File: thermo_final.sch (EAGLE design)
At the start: 113 parts

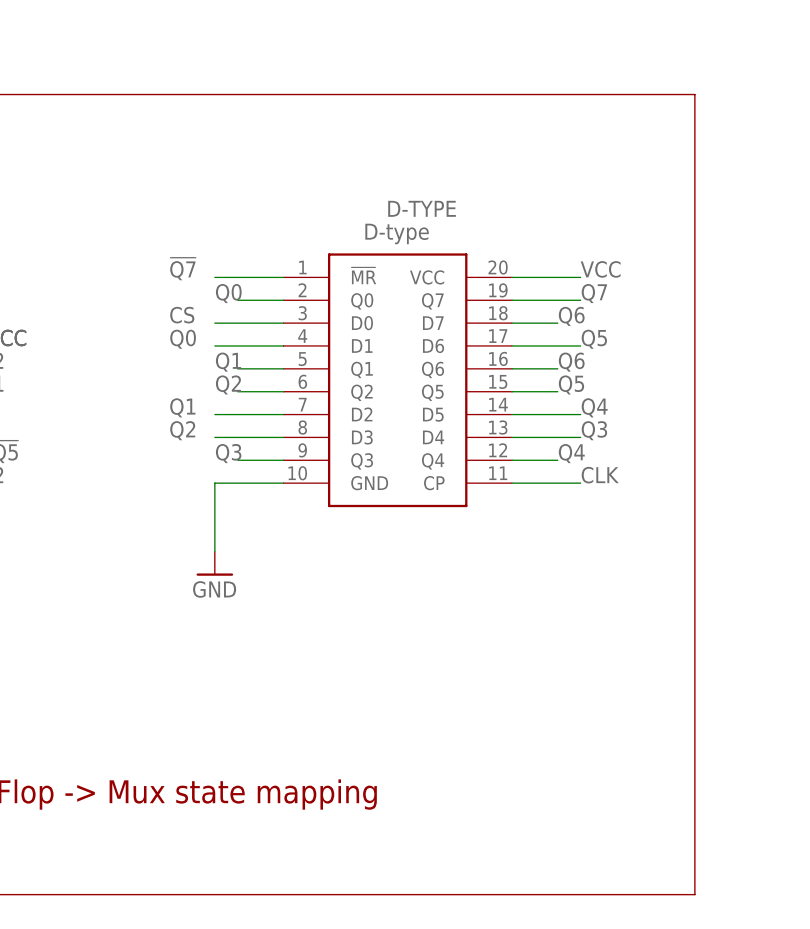
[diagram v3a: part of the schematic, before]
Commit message: Fixed Flip-Flop Footprint/Pushed 3D Model
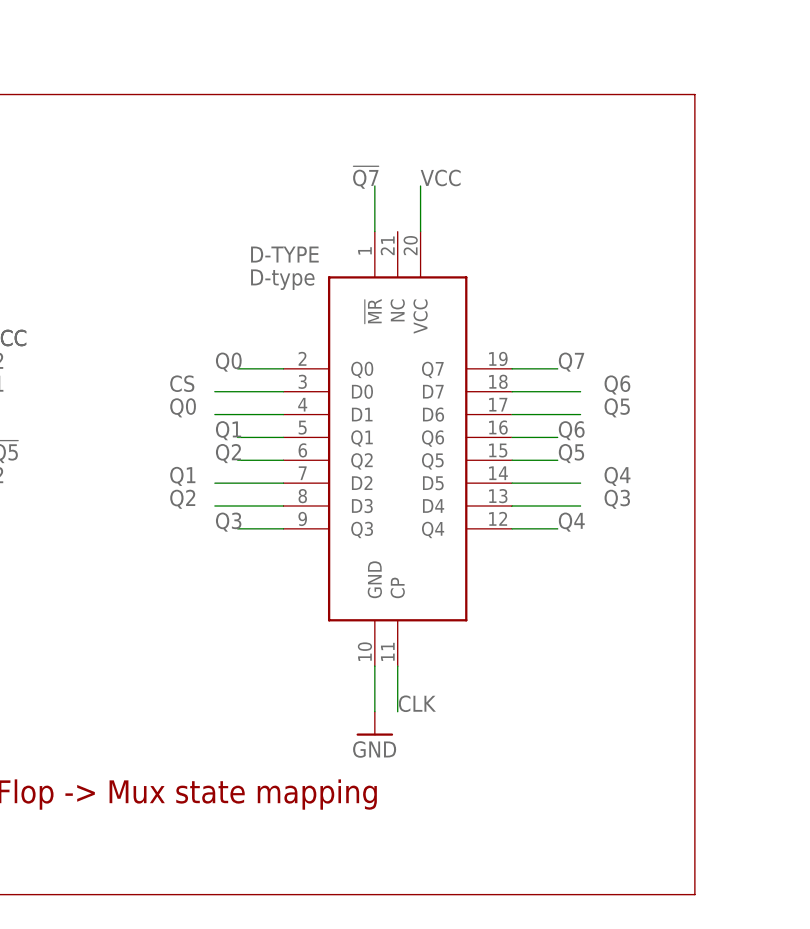
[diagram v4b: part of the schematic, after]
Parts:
- D-TYPE: device SamacSys_Parts:74AHCT273D,118 -> SamacSys_Parts:74AHC273BQ,115
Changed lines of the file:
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@@
 <part name="C1" library="SamacSys_Parts" library_urn="urn:adsk.eagle:library:34728992" deviceset="CGA3E2X7R1H104K080AE" device="" package3d_urn="urn:adsk.eagle:package:34729062/3" value="0.1uF"/>
 <part name="GND3" library="supply1" library_urn="urn:adsk.eagle:library:371" deviceset="GND" device=""/>
-<part name="D-TYPE" library="SamacSys_Parts" library_urn="urn:adsk.eagle:library:34728992" deviceset="74AHCT273D,118" device="" package3d_urn="urn:adsk.eagle:package:34729072/2" value="D-type"/>
+<part name="D-TYPE" library="SamacSys_Parts" library_urn="urn:adsk.eagle:library:34728992" deviceset="74AHC273BQ,115" device="" package3d_urn="urn:adsk.eagle:package:35179643/2" value="D-type"/>
 <part name="AND2" library="SamacSys_Parts" library_urn="urn:adsk.eagle:library:34728992" deviceset="SN74LVC08AMDREP" device="" package3d_urn="urn:adsk.eagle:package:34729073/2" value="AND1"/>
 <part name="GND5" library="supply1" library_urn="urn:adsk.eagle:library:371" deviceset="GND" device=""/>
@@
 <attribute name="VALUE" x="177.8" y="-22.86" size="1.778" layer="96"/>
 </instance>
-<instance part="D-TYPE" gate="G$1" x="15.24" y="-109.22" smashed="yes">
-<attribute name="NAME" x="26.67" y="-101.6" size="1.778" layer="95" align="center-left"/>
-<attribute name="VALUE" x="24.13" y="-104.14" size="1.778" layer="96" align="center-left"/>
+<instance part="D-TYPE" gate="G$1" x="15.24" y="-119.38" smashed="yes">
+<attribute name="NAME" x="11.43" y="-106.68" size="1.778" layer="95" align="center-left"/>
+<attribute name="VALUE" x="11.43" y="-109.22" size="1.778" layer="96" align="center-left"/>
 </instance>
 <instance part="AND2" gate="G$1" x="-114.3" y="-99.06" smashed="yes">
@@
 <attribute name="VALUE" x="-124.46" y="-127" size="1.778" layer="96"/>
 </instance>
-<instance part="GND6" gate="1" x="7.62" y="-142.24" smashed="yes">
-<attribute name="VALUE" x="5.08" y="-144.78" size="1.778" layer="96"/>
+<instance part="GND6" gate="1" x="25.4" y="-160.02" smashed="yes">
+<attribute name="VALUE" x="22.86" y="-162.56" size="1.778" layer="96"/>
 </instance>
 <instance part="INVERTER" gate="G$1" x="-172.72" y="-116.84" smashed="yes">
@@
 <segment>
 <pinref part="D-TYPE" gate="G$1" pin="GND"/>
-<wire x1="15.24" y1="-132.08" x2="7.62" y2="-132.08" width="0.1524" layer="91"/>
-<wire x1="7.62" y1="-132.08" x2="7.62" y2="-139.7" width="0.1524" layer="91"/>
+<wire x1="25.4" y1="-152.4" x2="25.4" y2="-157.48" width="0.1524" layer="91"/>
 <pinref part="GND6" gate="1" pin="GND"/>
 </segment>
@@
 <segment>
 <pinref part="D-TYPE" gate="G$1" pin="VCC"/>
-<wire x1="40.64" y1="-109.22" x2="48.26" y2="-109.22" width="0.1524" layer="91"/>
-<label x="48.26" y="-109.22" size="1.778" layer="95"/>
+<wire x1="30.48" y1="-104.14" x2="30.48" y2="-99.06" width="0.1524" layer="91"/>
+<label x="30.48" y="-99.06" size="1.778" layer="95"/>
 </segment>
 <segment>
@@
 <segment>
 <pinref part="D-TYPE" gate="G$1" pin="CP"/>
-<wire x1="40.64" y1="-132.08" x2="48.26" y2="-132.08" width="0.1524" layer="91"/>
-<label x="48.26" y="-132.08" size="1.778" layer="95"/>
+<wire x1="27.94" y1="-152.4" x2="27.94" y2="-157.48" width="0.1524" layer="91"/>
+<label x="27.94" y="-157.48" size="1.778" layer="95"/>
 </segment>
 <segment>
@@
 <segment>
 <pinref part="D-TYPE" gate="G$1" pin="D0"/>
-<wire x1="15.24" y1="-114.3" x2="7.62" y2="-114.3" width="0.1524" layer="91"/>
-<label x="2.54" y="-114.3" size="1.778" layer="95"/>
+<wire x1="15.24" y1="-121.92" x2="7.62" y2="-121.92" width="0.1524" layer="91"/>
+<label x="2.54" y="-121.92" size="1.778" layer="95"/>
 </segment>
 <segment>
@@
 <segment>
 <pinref part="D-TYPE" gate="G$1" pin="D7"/>
-<wire x1="40.64" y1="-114.3" x2="45.72" y2="-114.3" width="0.1524" layer="91"/>
-<label x="45.72" y="-114.3" size="1.778" layer="95"/>
+<wire x1="40.64" y1="-121.92" x2="48.26" y2="-121.92" width="0.1524" layer="91"/>
+<label x="50.8" y="-121.92" size="1.778" layer="95"/>
 </segment>
 <segment>
 <pinref part="D-TYPE" gate="G$1" pin="Q6"/>
-<wire x1="40.64" y1="-119.38" x2="45.72" y2="-119.38" width="0.1524" layer="91"/>
-<label x="45.72" y="-119.38" size="1.778" layer="95"/>
+<wire x1="40.64" y1="-127" x2="45.72" y2="-127" width="0.1524" layer="91"/>
+<label x="45.72" y="-127" size="1.778" layer="95"/>
 </segment>
 <segment>
@@
 <segment>
 <pinref part="D-TYPE" gate="G$1" pin="D6"/>
-<wire x1="40.64" y1="-116.84" x2="48.26" y2="-116.84" width="0.1524" layer="91"/>
-<label x="48.26" y="-116.84" size="1.778" layer="95"/>
+<wire x1="40.64" y1="-124.46" x2="48.26" y2="-124.46" width="0.1524" layer="91"/>
+<label x="50.8" y="-124.46" size="1.778" layer="95"/>
 </segment>
 <segment>
 <pinref part="D-TYPE" gate="G$1" pin="Q5"/>
-<wire x1="40.64" y1="-121.92" x2="45.72" y2="-121.92" width="0.1524" layer="91"/>
-<label x="45.72" y="-121.92" size="1.778" layer="95"/>
+<wire x1="40.64" y1="-129.54" x2="45.72" y2="-129.54" width="0.1524" layer="91"/>
+<label x="45.72" y="-129.54" size="1.778" layer="95"/>
 </segment>
 <segment>
@@
 <segment>
 <pinref part="D-TYPE" gate="G$1" pin="D5"/>
-<wire x1="40.64" y1="-124.46" x2="48.26" y2="-124.46" width="0.1524" layer="91"/>
-<label x="48.26" y="-124.46" size="1.778" layer="95"/>
+<wire x1="40.64" y1="-132.08" x2="48.26" y2="-132.08" width="0.1524" layer="91"/>
+<label x="50.8" y="-132.08" size="1.778" layer="95"/>
 </segment>
 <segment>
 <pinref part="D-TYPE" gate="G$1" pin="Q4"/>
-<wire x1="40.64" y1="-129.54" x2="45.72" y2="-129.54" width="0.1524" layer="91"/>
-<label x="45.72" y="-129.54" size="1.778" layer="95"/>
+<wire x1="40.64" y1="-137.16" x2="45.72" y2="-137.16" width="0.1524" layer="91"/>
+<label x="45.72" y="-137.16" size="1.778" layer="95"/>
 </segment>
 <segment>
@@
 <segment>
 <pinref part="D-TYPE" gate="G$1" pin="D4"/>
-<wire x1="40.64" y1="-127" x2="48.26" y2="-127" width="0.1524" layer="91"/>
-<label x="48.26" y="-127" size="1.778" layer="95"/>
+<wire x1="40.64" y1="-134.62" x2="48.26" y2="-134.62" width="0.1524" layer="91"/>
+<label x="50.8" y="-134.62" size="1.778" layer="95"/>
 </segment>
 <segment>
 <pinref part="D-TYPE" gate="G$1" pin="Q3"/>
-<wire x1="15.24" y1="-129.54" x2="10.16" y2="-129.54" width="0.1524" layer="91"/>
-<label x="7.62" y="-129.54" size="1.778" layer="95"/>
+<wire x1="15.24" y1="-137.16" x2="10.16" y2="-137.16" width="0.1524" layer="91"/>
+<label x="7.62" y="-137.16" size="1.778" layer="95"/>
 </segment>
 <segment>
@@
 <segment>
 <pinref part="D-TYPE" gate="G$1" pin="D1"/>
-<wire x1="15.24" y1="-116.84" x2="7.62" y2="-116.84" width="0.1524" layer="91"/>
-<label x="2.54" y="-116.84" size="1.778" layer="95"/>
+<wire x1="15.24" y1="-124.46" x2="7.62" y2="-124.46" width="0.1524" layer="91"/>
+<label x="2.54" y="-124.46" size="1.778" layer="95"/>
 </segment>
 <segment>
 <pinref part="D-TYPE" gate="G$1" pin="Q0"/>
-<wire x1="15.24" y1="-111.76" x2="10.16" y2="-111.76" width="0.1524" layer="91"/>
-<label x="7.62" y="-111.76" size="1.778" layer="95"/>
+<wire x1="15.24" y1="-119.38" x2="10.16" y2="-119.38" width="0.1524" layer="91"/>
+<label x="7.62" y="-119.38" size="1.778" layer="95"/>
 </segment>
 <segment>
@@
 <segment>
 <pinref part="D-TYPE" gate="G$1" pin="D2"/>
-<wire x1="15.24" y1="-124.46" x2="7.62" y2="-124.46" width="0.1524" layer="91"/>
-<label x="2.54" y="-124.46" size="1.778" layer="95"/>
+<wire x1="15.24" y1="-132.08" x2="7.62" y2="-132.08" width="0.1524" layer="91"/>
+<label x="2.54" y="-132.08" size="1.778" layer="95"/>
 </segment>
 <segment>
 <pinref part="D-TYPE" gate="G$1" pin="Q1"/>
-<wire x1="15.24" y1="-119.38" x2="10.16" y2="-119.38" width="0.1524" layer="91"/>
-<label x="7.62" y="-119.38" size="1.778" layer="95"/>
+<wire x1="15.24" y1="-127" x2="10.16" y2="-127" width="0.1524" layer="91"/>
+<label x="7.62" y="-127" size="1.778" layer="95"/>
 </segment>
 <segment>
@@
 <segment>
 <pinref part="D-TYPE" gate="G$1" pin="D3"/>
-<wire x1="15.24" y1="-127" x2="7.62" y2="-127" width="0.1524" layer="91"/>
-<label x="2.54" y="-127" size="1.778" layer="95"/>
+<wire x1="15.24" y1="-134.62" x2="7.62" y2="-134.62" width="0.1524" layer="91"/>
+<label x="2.54" y="-134.62" size="1.778" layer="95"/>
 </segment>
 <segment>
 <pinref part="D-TYPE" gate="G$1" pin="Q2"/>
-<wire x1="15.24" y1="-121.92" x2="10.16" y2="-121.92" width="0.1524" layer="91"/>
-<label x="7.62" y="-121.92" size="1.778" layer="95"/>
+<wire x1="15.24" y1="-129.54" x2="10.16" y2="-129.54" width="0.1524" layer="91"/>
+<label x="7.62" y="-129.54" size="1.778" layer="95"/>
 </segment>
 <segment>
@@
 <segment>
 <pinref part="D-TYPE" gate="G$1" pin="Q7"/>
-<wire x1="40.64" y1="-111.76" x2="48.26" y2="-111.76" width="0.1524" layer="91"/>
-<label x="48.26" y="-111.76" size="1.778" layer="95"/>
+<wire x1="40.64" y1="-119.38" x2="45.72" y2="-119.38" width="0.1524" layer="91"/>
+<label x="45.72" y="-119.38" size="1.778" layer="95"/>
 </segment>
 <segment>
@@
 <segment>
 <pinref part="D-TYPE" gate="G$1" pin="!MR"/>
-<wire x1="15.24" y1="-109.22" x2="7.62" y2="-109.22" width="0.1524" layer="91"/>
-<label x="2.54" y="-109.22" size="1.778" layer="95"/>
-</segment>
-</net>
+<wire x1="25.4" y1="-104.14" x2="25.4" y2="-99.06" width="0.1524" layer="91"/>
+<label x="22.86" y="-99.06" size="1.778" layer="95"/>
+</segment>
+</net>

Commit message: Added CMRR Caps at CJ input (Finalized)
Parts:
- added C11, C12: 06035C270JAT2A, SamacSys_Parts:06035C270JAT2A
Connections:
- net CJ+: now also C12.1
- net CJ-: now also C11.2
- net GND: now also C11.1, C12.2
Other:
- note added: "CMRR Aliasing Filter"
- moved on the sheet: AND1, AND2, C1, C10, C2, C3, C4, C5, C6, C7, C8, C9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

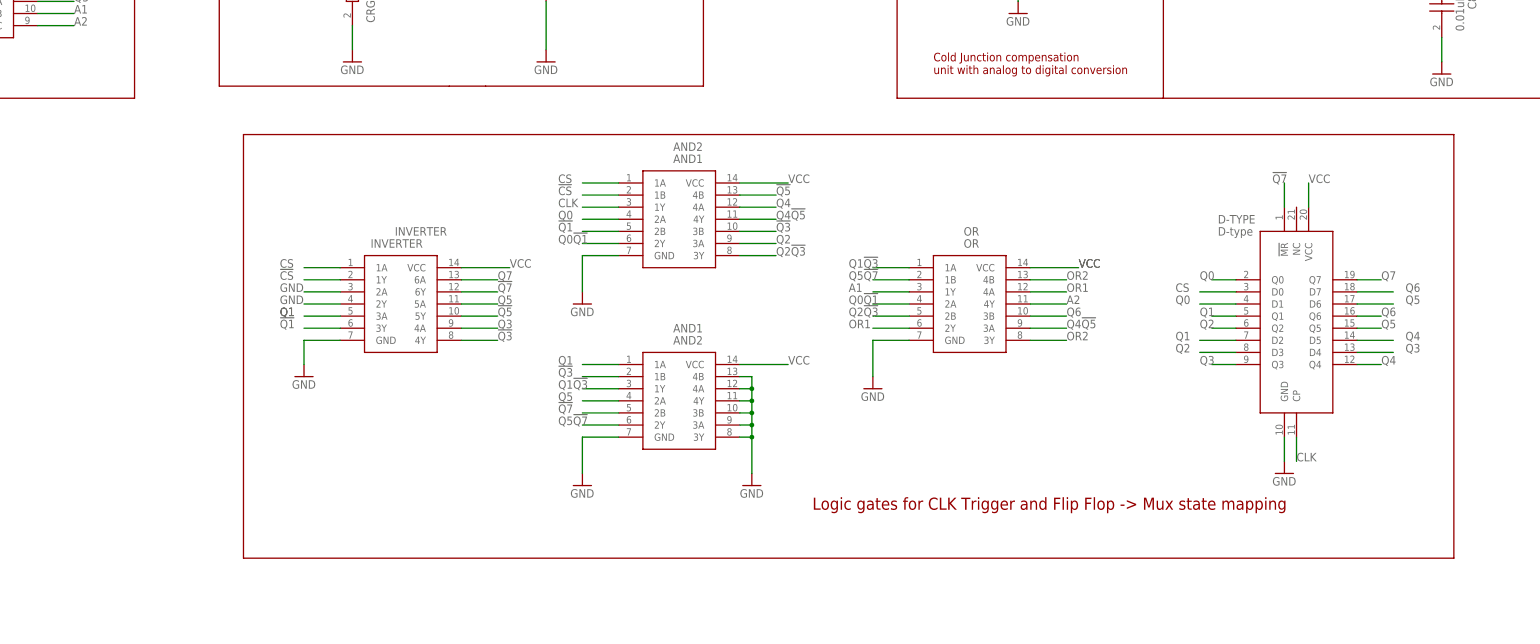
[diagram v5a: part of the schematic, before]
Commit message: Final board/3d model with delay trigger fix
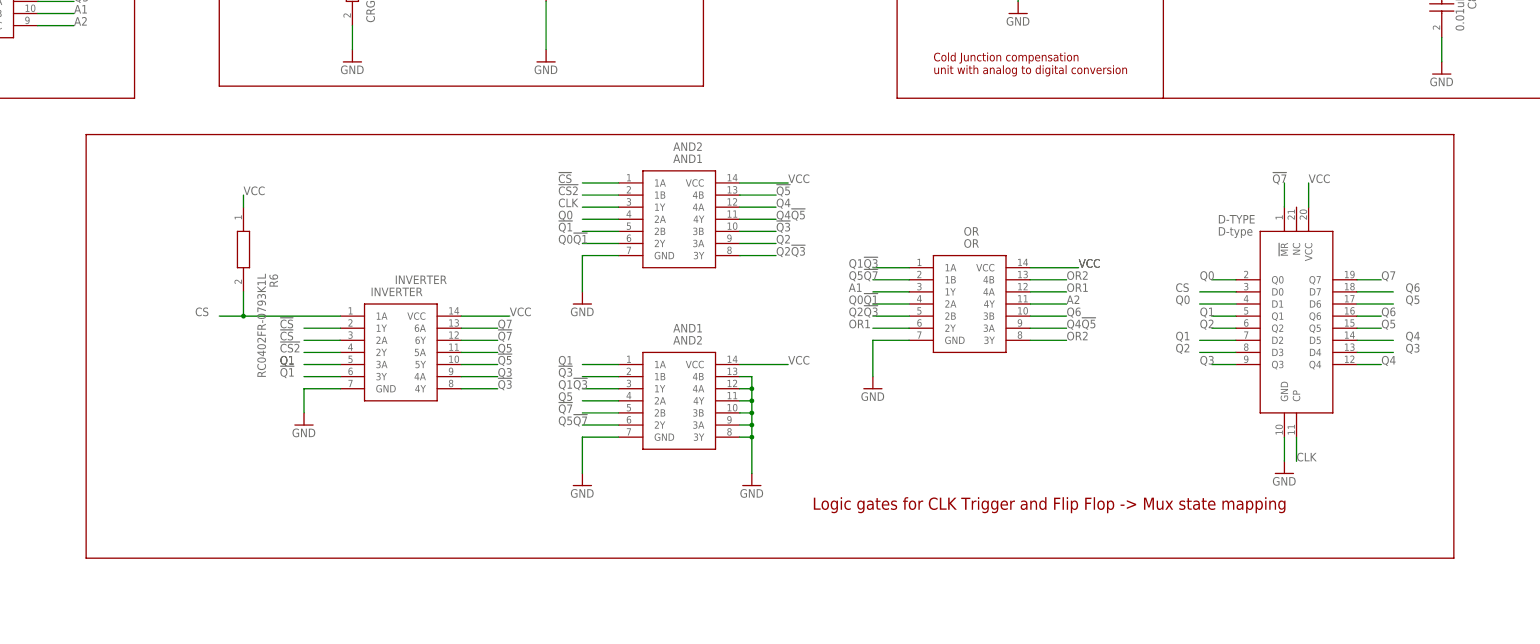
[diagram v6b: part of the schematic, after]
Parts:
- added R6: RC0402FR-0793K1L, SamacSys_Parts:RC0402FR-0793K1L
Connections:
- new net !CS2: AND2.1B, INVERTER.2Y
- net !CS: now also AND2.1A, INVERTER.2A; no longer AND2.1B
- net CS: now also R6.2; no longer AND2.1A
- net GND: no longer INVERTER.2A, INVERTER.2Y
- net VCC: now also R6.1
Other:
- moved on the sheet: INVERTER
